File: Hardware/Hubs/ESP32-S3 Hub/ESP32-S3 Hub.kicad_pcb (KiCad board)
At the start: 6 copper layers, 15 x 30 mm, 61 parts, among them J1 1.27mm 3pin socket, J10 1.27mm 3pin socket, J11 7 pin FPC 0.3mm Panasonic Y3b, J12 1.27mm 3pin socket, J13 TE 3-2363961-0 receptacle, J14 TE 3-2363962-0 Connector, J16 TE 3-2363961-0 receptacle, J17 TE 3-2363962-0 Connector, J2 1.27mm 3pin socket, J21 1.27mm 4 pin socket, J22 1.27mm 4 pin header, J3 7 pin FPC 0.3mm Panasonic Y3b, J4 1.27mm 3pin socket, J5 7 pin FPC 0.3mm Panasonic Y3b, J6 1.27mm 3pin socket, J7 1.27mm 3pin socket, J8 7 pin FPC 0.3mm Panasonic Y3b, J9 1.27mm 3pin socket, SW1 Mitsumi R-667996, SW2 Mitsumi R-667996, U1 ESP32-S3, U2 74HC595, U3 THVD1420DRLR, Y1 ABM11-40.000MHZ-B1U-T3, 10ppm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

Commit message: Started Proto 2 again
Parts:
- C11, C12, Y1: moved to B.Cu
- R1: moved to F.Cu
- moved Y1 9.28 mm to (152.5, 98.0), turned to 0 degrees
- moved C12 9.13 mm to (152.3, 96.2), turned to 0 degrees
- moved C11 8.86 mm to (151.2, 99.8), turned to 180 degrees
- moved TP12 7.75 mm to (165.6, 99.1)
- moved TP1 6.31 mm to (164.6, 91.7)
- moved TP14 6.02 mm to (165.8, 96.2)
- moved R6 4.32 mm to (150.8, 98.0), turned to 90 degrees
- moved C6 3.16 mm to (150.9, 99.5)
- moved R1 2.02 mm to (155.4, 101.5), turned to 180 degrees
- moved U1 0.86 mm to (155.9, 96.0), turned to 90 degrees
- moved R5 0.43 mm to (151.7, 94.7)
- moved U2 0.32 mm to (155.9, 97.0), turned to 0 degrees
- moved C2 0.25 mm to (151.7, 100.8)
- moved C3 0.20 mm to (151.6, 101.8)
- turned C4 to 180 degrees
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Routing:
- net VDD: track 162.3 -> 25.5 mm, vias 9 -> 1
- net SCL1: track 52.0 -> 0.00 mm, vias 5 -> 0
- net SDA1: track 46.8 -> 0.00 mm, vias 5 -> 0
- net CS8: track 32.3 -> 0.00 mm, vias 3 -> 0
- net CS7: track 32.3 -> 0.01 mm, vias 3 -> 0
- net Free1: track 31.4 -> 0.00 mm, vias 3 -> 0
- net CS6: track 27.2 -> 0.00 mm, vias 3 -> 0
- net LED: track 24.3 -> 0.00 mm, vias 2 -> 0
- net 4C: track 24.3 -> 0.00 mm, vias 1 -> 0
- net 2C: track 23.5 -> 0.00 mm, vias 1 -> 0
- net CS5: track 22.3 -> 0.00 mm, vias 3 -> 0
- net MOSI1: track 89.5 -> 67.6 mm
- net 2B: track 21.3 -> 0.00 mm, vias 1 -> 0
- net 4A: track 19.5 -> 0.00 mm, vias 1 -> 0
- net Free2: track 19.3 -> 0.00 mm, vias 3 -> 0
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- removed copper zone on F.Cu, net Net-(C4-Pad1)
- removed copper zone on F.Cu, net VDD

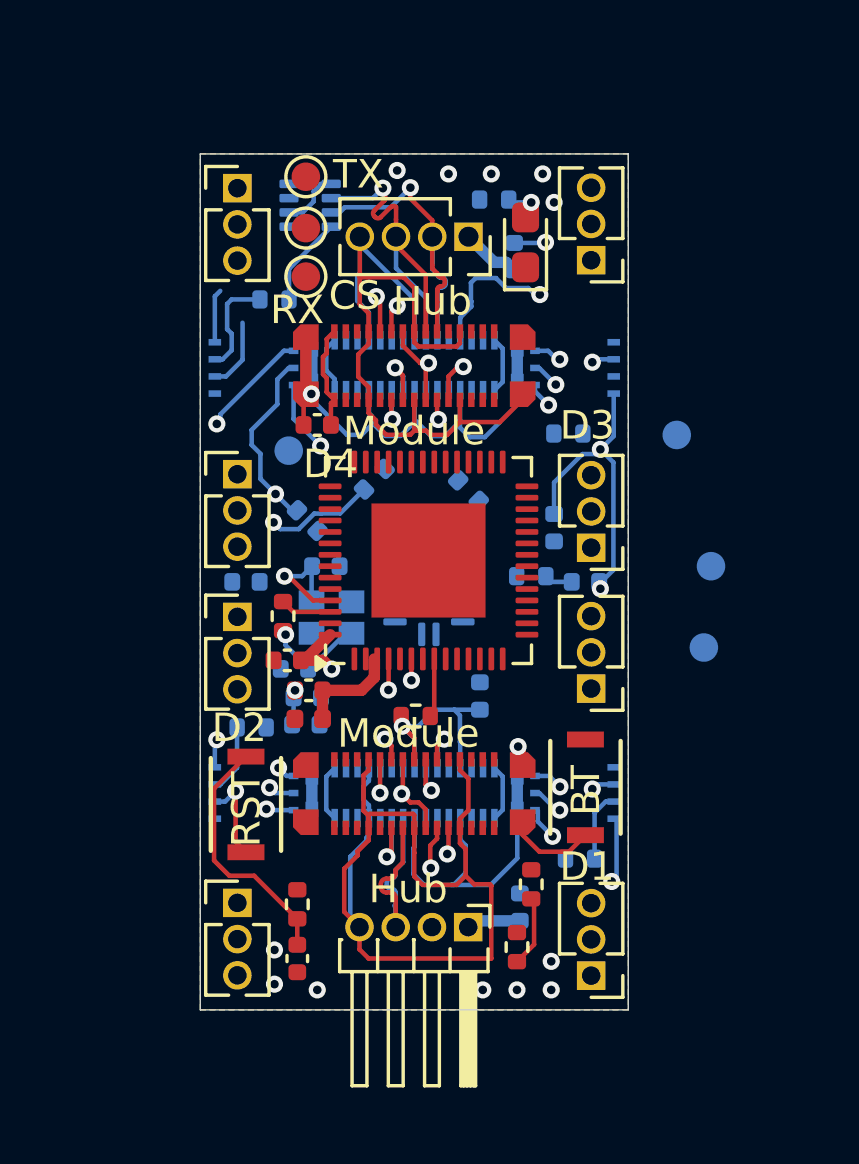
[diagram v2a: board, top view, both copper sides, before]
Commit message: Updated connectors in schem and pcb
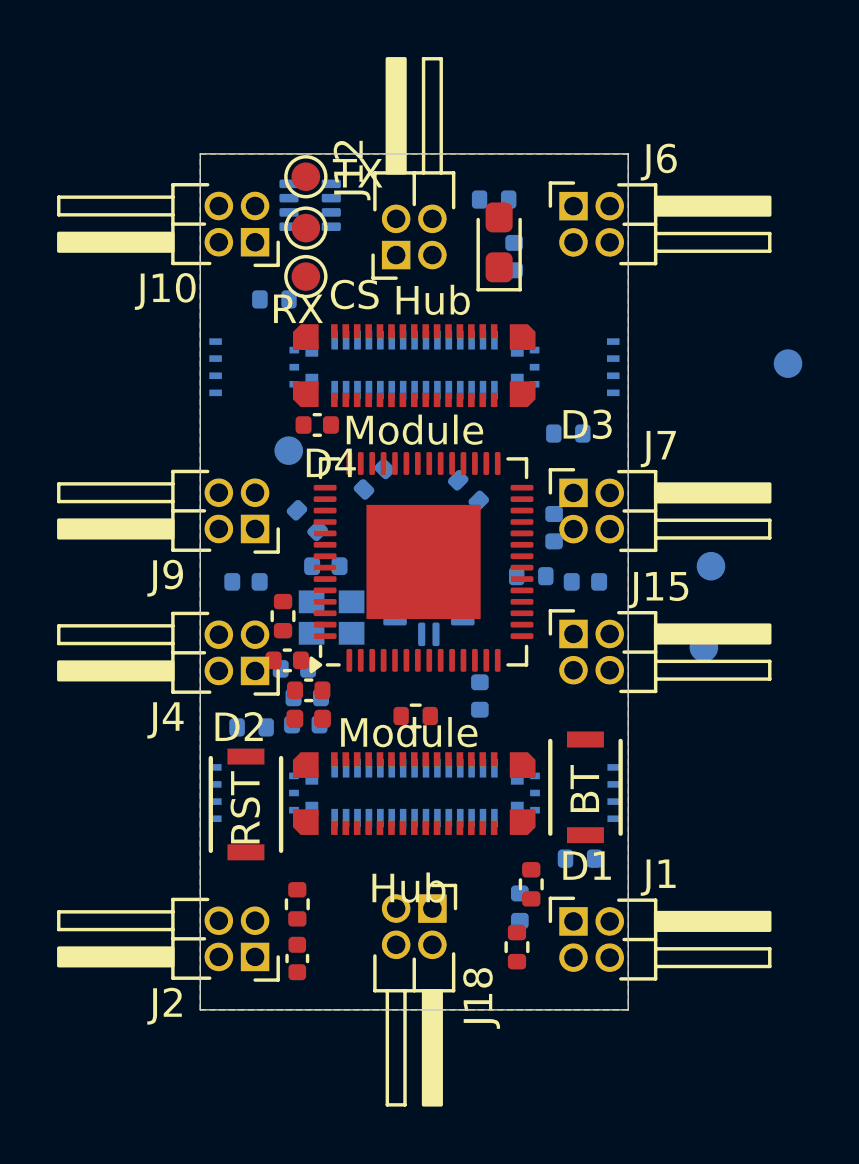
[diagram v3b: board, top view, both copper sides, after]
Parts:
- removed J21: 1.27mm 4 pin socket, Connector_PinSocket_1.27mm:PinSocket_1x04_P1.27mm_Vertical
- removed J22: 1.27mm 4 pin header, Connector_PinHeader_1.27mm:PinHeader_1x04_P1.27mm_Horizontal
- added J15: Precidip 853-87-004-20-001101, Connector_PinHeader_1.27mm:PinHeader_2x02_P1.27mm_Horizontal, F.Cu at (161.0, 98.6)
- added J18: Precidip 852-10-004-20-001101, Connector_PinHeader_1.27mm:PinHeader_2x02_P1.27mm_Horizontal, F.Cu at (156.0, 108.2)
- J1, J10, J12, J2, J4, J6, J7, J9: value 1.27mm 3pin socket -> Precidip 853-87-004-20-001101; footprint Connector_PinHeader_1.27mm:PinHeader_1x03_P1.27mm_Vertical -> Connector_PinHeader_1.27mm:PinHeader_2x02_P1.27mm_Horizontal
- J11, J3, J5, J8: value 7 pin FPC 0.3mm Panasonic Y3b -> 7 pin FPC 0.3mm Aces 51688-0070M-001; footprint custom_Interface_HID:fpc_7pin_0.3mm_connector Panasonic -> custom_Connector:fpc_7pin_0.3mm_connector Aces
- moved J6 18.6 mm to (161.0, 83.6)
- moved J2 11.8 mm to (149.8, 109.9)
- moved J9 11.8 mm to (149.8, 94.9)
- moved J1 8.18 mm to (161.0, 108.7), turned to 0 degrees
- moved J7 8.18 mm to (161.0, 93.7), turned to 0 degrees
- moved J10 8.15 mm to (149.8, 84.9), turned to 180 degrees
- moved J4 8.15 mm to (149.8, 99.9), turned to 180 degrees
- moved J12 6.04 mm to (154.8, 85.3), turned to 90 degrees
- moved TP1 4.63 mm to (168.5, 89.2)
- moved D1 0.93 mm to (158.4, 84.9)
- moved U1 0.18 mm to (155.7, 96.1)
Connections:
- J1 pad 1: 1A -> 1CSA-A
- J1 pad 2: 1B -> 1CSA-B
- J1 pad 3: 1C -> unconnected-(J1-Pin_3-Pad3)
- J10 pad 1: 4A -> 4CSA-A
- J10 pad 2: 4B -> 4CSA-B
- J10 pad 3: 4C -> unconnected-(J10-Pin_3-Pad3)
- J12 pad 1: 4CSA-A -> RS485-
- J12 pad 2: 4CSA-B -> GND
- J12 pad 3: unconnected-(J12-Pin_3-Pad3) -> RS485+
- J2 pad 1: 1CSA-A -> 2A
- J2 pad 2: 1CSA-B -> 2B
- J2 pad 3: unconnected-(J2-Pin_3-Pad3) -> 2C
- J4 pad 1: 2A -> 2CSA-A
- J4 pad 2: 2B -> 2CSA-B
- J4 pad 3: 2C -> unconnected-(J4-Pin_3-Pad3)
- J6 pad 1: 2CSA-A -> 3A
- J6 pad 2: 2CSA-B -> 3B
- J6 pad 3: unconnected-(J6-Pin_3-Pad3) -> 3C
- J7 pad 1: 3A -> 3CSA-A
- J7 pad 2: 3B -> 3CSA-B
- J7 pad 3: 3C -> unconnected-(J7-Pin_3-Pad3)
- J9 pad 1: 3CSA-A -> 4A
- J9 pad 2: 3CSA-B -> 4B
- J9 pad 3: unconnected-(J9-Pin_3-Pad3) -> 4C
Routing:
- net GND: track 140.1 -> 0.00 mm, vias 25 -> 0
- net MISO1: track 95.1 -> 0.00 mm, vias 8 -> 0
- net MOSI1: track 67.6 -> 0.00 mm, vias 9 -> 0
- net RS485+: track 65.4 -> 0.00 mm, vias 4 -> 0
- net SCK1: track 60.1 -> 0.00 mm, vias 6 -> 0
- net RS485-: track 69.0 -> 16.8 mm, vias 3 -> 0
- net VDD: track 25.5 -> 0.20 mm, vias 1 -> 0
- net NRST: track 9.87 -> 0.00 mm, vias 1 -> 0
- net Net-(U1-XTAL_N): track 4.25 -> 0.00 mm, vias 1 -> 0
- net Net-(C11-Pad1): track 3.74 -> 0.00 mm, vias 1 -> 0
- net Net-(C4-Pad1): track 3.66 -> 0.00 mm
- net CS4: track 3.63 -> 0.00 mm
- net CS1: track 2.54 -> 0.00 mm
- net CS2: track 2.44 -> 0.00 mm
- net Net-(U1-GPIO3): track 2.06 -> 0.00 mm
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
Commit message: Updated component arrangements and fixed pinout on upstream port
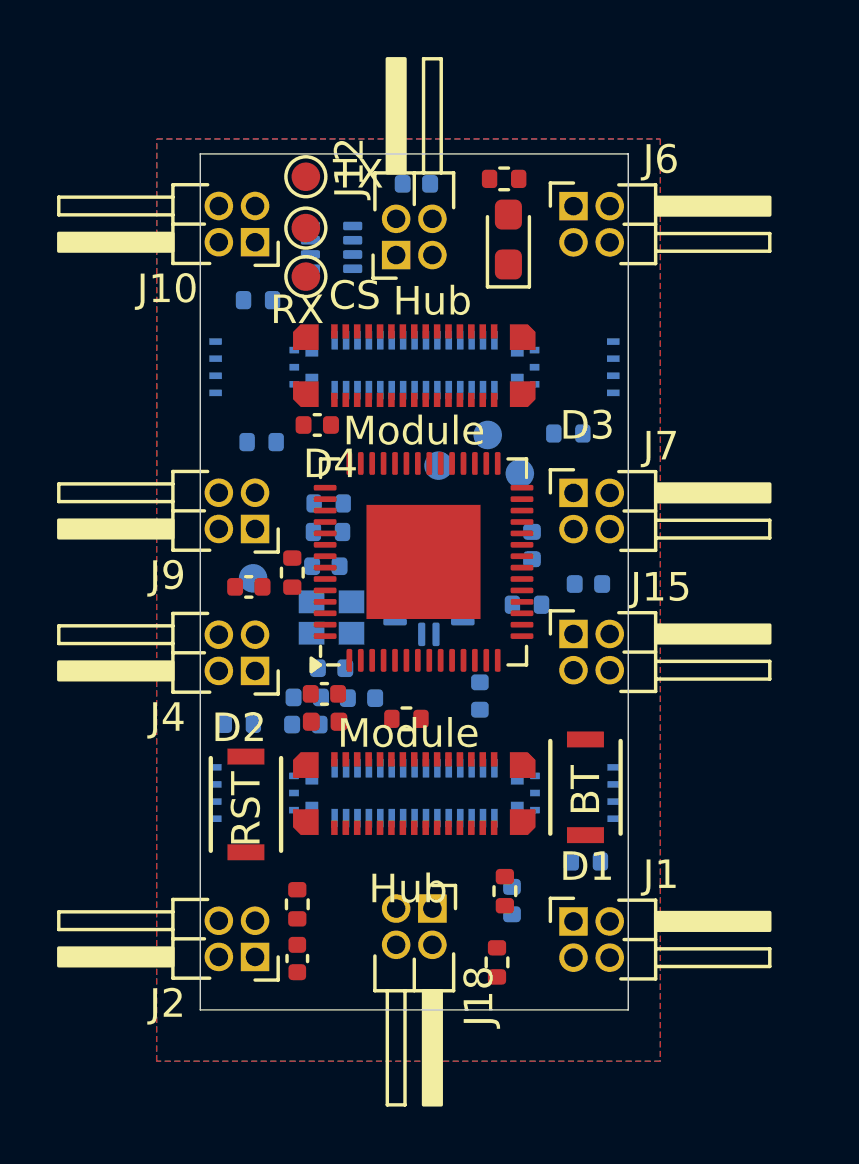
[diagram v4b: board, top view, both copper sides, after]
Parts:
- C6: moved to B.Cu
- C9, R10: moved to F.Cu
- moved TP1 10.8 mm to (158.0, 91.7)
- moved TP14 10.2 mm to (156.2, 92.7), turned to 0 degrees
- moved TP12 8.88 mm to (159.1, 93.0), turned to 0 degrees
- moved R3 7.45 mm to (150.1, 91.9), turned to 0 degrees
- moved TP4 4.65 mm to (149.8, 96.7)
- moved C1 4.27 mm to (155.5, 82.8), turned to 180 degrees
- moved C6 2.92 mm to (153.6, 100.9), turned to 180 degrees
- moved R4 1.81 mm to (152.4, 94.0), turned to 0 degrees
- moved U3 1.65 mm to (152.5, 85.1)
- moved R6 1.56 mm to (151.1, 96.5), turned to -90 degrees
- moved C11 1.30 mm to (152.5, 99.8)
- moved R11 1.01 mm to (159.3, 97.6)
- moved C7 1.00 mm to (159.5, 95.5)
- moved R8 0.96 mm to (158.6, 107.6)
- moved R9 0.88 mm to (158.3, 110.1)
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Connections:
- J18 pad 1: VDD -> RS485+
- J18 pad 2: RS485+ -> VDD
- J18 pad 3: GND -> RS485-
- J18 pad 4: RS485- -> GND
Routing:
- net RS485-: track 16.8 -> 0.00 mm
- net GND: track 0.00 -> 16.8 mm

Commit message: Add 5mil traces & 0.4mm vias, started via placement
I am decreasing the size further to speed up routing and avoid pain. The cost will be higher, but not that much higher from 0.3mm to 0.2mm and 0.6mm to 0.4mm vias. I can route more items.
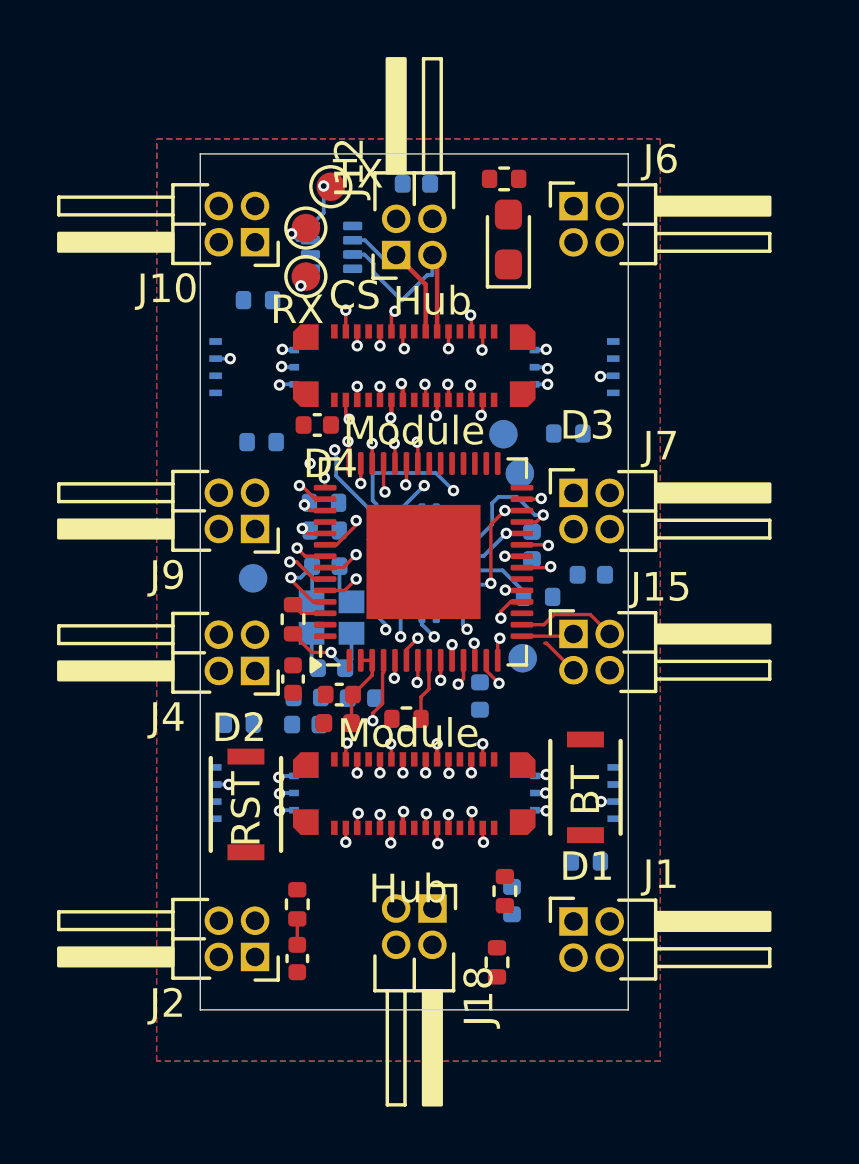
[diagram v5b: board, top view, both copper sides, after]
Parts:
- removed J14, J17: TE 3-2363962-0 Connector, custom_testpoints:TE_mezzanine_conn_3-2363962-0
- moved TP14 7.37 mm to (159.2, 99.5)
- moved C9 3.58 mm to (151.2, 100.2), turned to 90 degrees
- moved R6 1.64 mm to (151.2, 98.1), turned to 90 degrees
- moved TP3 0.94 mm to (152.5, 83.0)
- moved U2 0.80 mm to (155.9, 96.1)
- moved TP1 0.55 mm to (158.5, 91.6)
- moved C4 0.52 mm to (152.8, 100.8)
- moved R11 0.48 mm to (159.7, 97.3)
- moved FB1 0.44 mm to (152.7, 101.8)
- moved C5 0.34 mm to (161.6, 96.5)
- moved R4 0.17 mm to (152.2, 94.0)
- moved R5 0.13 mm to (152.3, 95.0)
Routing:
- net GND: track 16.8 -> 2.74 mm
- net RS485-: track 0.00 -> 12.6 mm, vias 0 -> 3
- net RS485+: track 0.00 -> 11.2 mm, vias 0 -> 3
- net CS7: track 0.00 -> 7.45 mm, vias 0 -> 3
- net CS6: track 0.00 -> 5.80 mm, vias 0 -> 3
- net ShiftCLK: track 0.00 -> 5.01 mm, vias 0 -> 1
- net ShiftData: track 0.00 -> 4.35 mm, vias 0 -> 2
- net MOSI1: track 0.00 -> 4.29 mm, vias 0 -> 8
- net SCK1: track 0.00 -> 4.05 mm, vias 0 -> 8
- net MISO1: track 0.00 -> 3.83 mm, vias 0 -> 8
- net Net-(U1-XTAL_N): track 0.00 -> 3.76 mm, vias 0 -> 1
- net Net-(C11-Pad1): track 0.00 -> 3.68 mm, vias 0 -> 1
- net 1B: track 0.00 -> 3.50 mm
- net ShiftEn: track 0.00 -> 3.31 mm, vias 0 -> 1
- net SDA1: track 0.00 -> 3.23 mm, vias 0 -> 5
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
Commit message: Fix some track sizes and clearance issues
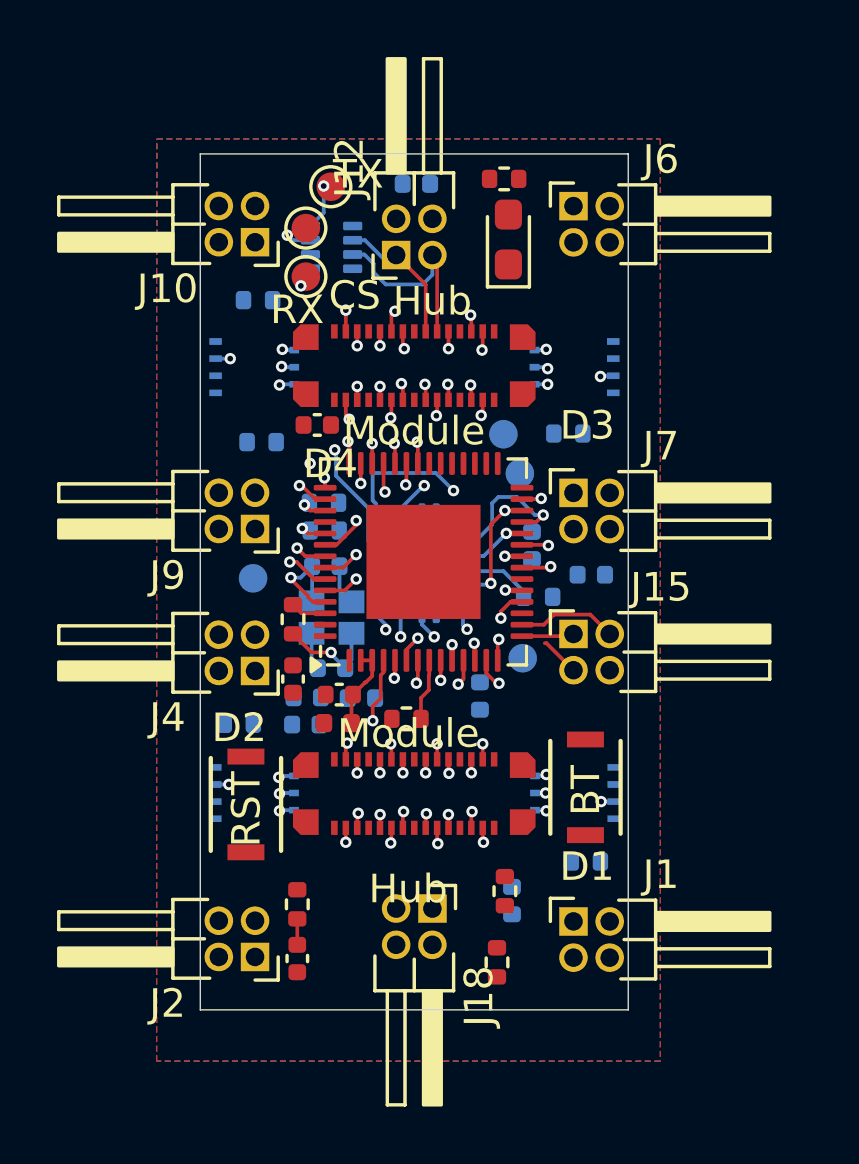
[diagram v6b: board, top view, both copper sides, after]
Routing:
- net RS485-: track 12.6 -> 6.73 mm
- net RS485+: track 11.2 -> 8.71 mm
